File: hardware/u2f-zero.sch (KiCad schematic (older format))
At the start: 16 parts, among them SW1 SW_PUSH

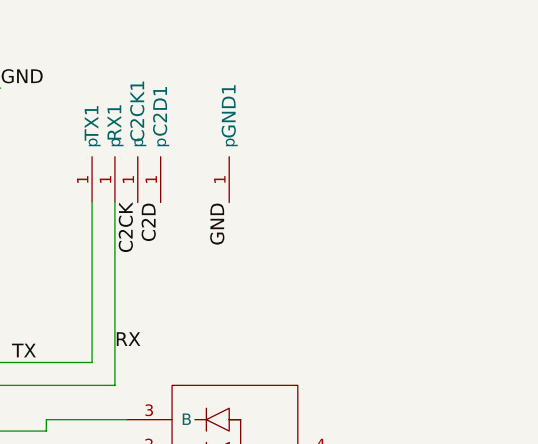
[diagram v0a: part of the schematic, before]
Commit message: changed usb connector from pcb connector to surface soldered connector
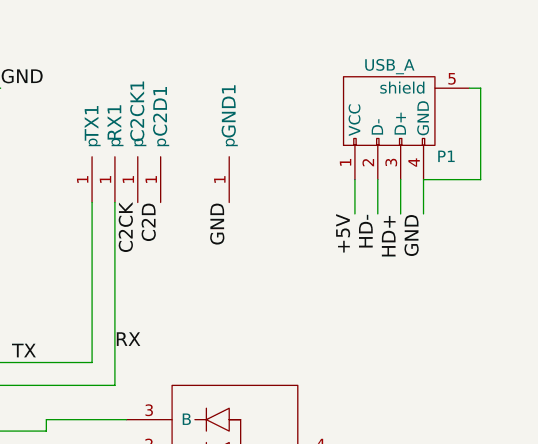
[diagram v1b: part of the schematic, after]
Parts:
- added P1: USB_A, footprints:USB_A_CON, symbol USB_A
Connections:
- net +5V: now also P1.1 (VCC)
- net GND: now also P1.4 (GND), P1.5 (shield)
- net HD+: now also P1.3 (D+)
- net HD-: now also P1.2 (D-)
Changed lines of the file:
@@
 	1    0    0    -1
 $EndComp
+$Comp
+L USB_A P1
+U 1 1 57F2AB61
+P 7800 3000
+F 0 "P1" H 8000 2800 50  0000 C CNN
+F 1 "USB_A" H 7750 3200 50  0000 C CNN
+F 2 "footprints:USB_A_CON" V 7750 2900 50  0001 C CNN
+F 3 "" V 7750 2900 50  0000 C CNN
+	1    7800 3000
+	1    0    0    -1
+$EndComp
+Wire Wire Line
+	8100 2900 8150 2900
+Wire Wire Line
+	8150 2900 8150 3300
+Wire Wire Line
+	8150 3300 7900 3300
+Wire Wire Line
+	7900 3300 7900 3450
+Text Label 7900 3450 3    60   ~ 0
+GND
+Text Label 7700 3450 3    60   ~ 0
+HD-
+Text Label 7800 3450 3    60   ~ 0
+HD+
+Text Label 7600 3450 3    60   ~ 0
++5V
+Wire Wire Line
+	7600 3300 7600 3450
+Wire Wire Line
+	7700 3300 7700 3450
+Wire Wire Line
+	7800 3300 7800 3450
 $EndSCHEMATC
